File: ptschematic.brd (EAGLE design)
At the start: 100 x 80 mm, 28 parts, among them U3 NCP1117LPST33T3G, U4 BGM13S, Y2 32MHz

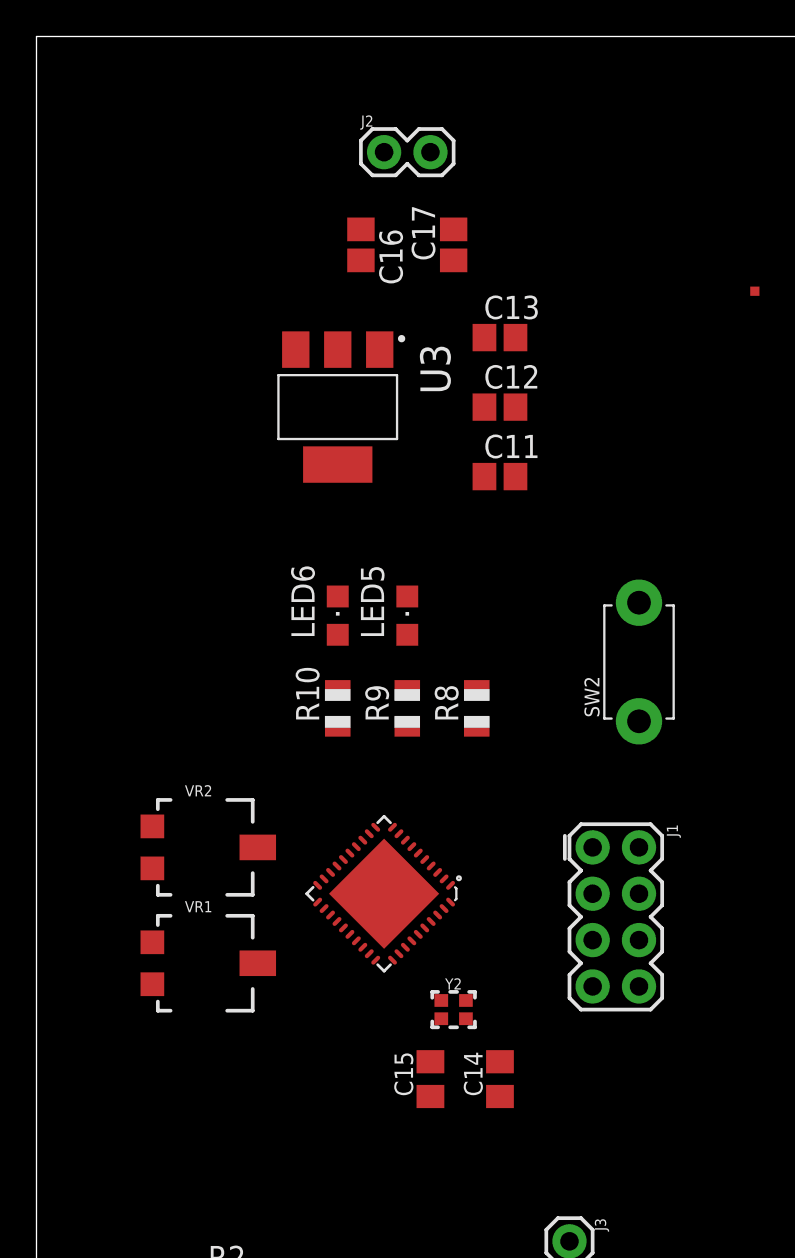
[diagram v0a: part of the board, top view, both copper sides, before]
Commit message: Started board routing
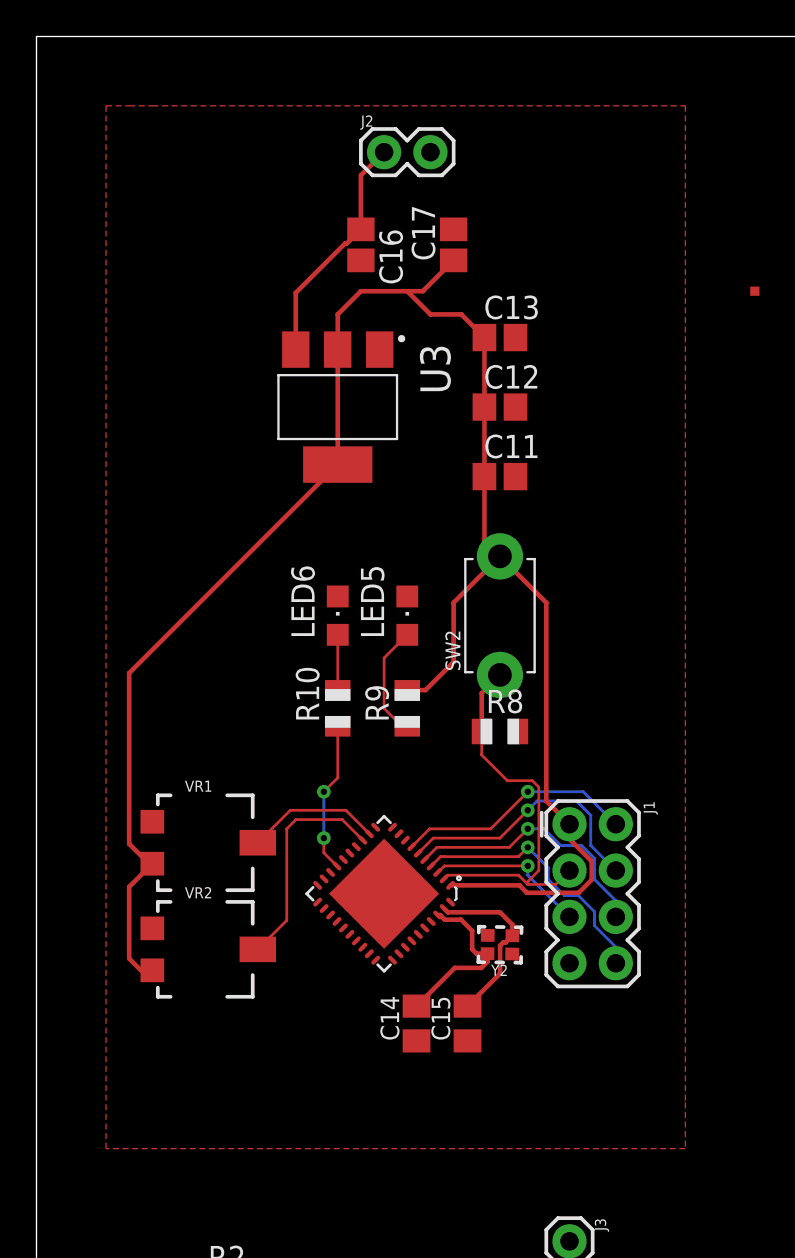
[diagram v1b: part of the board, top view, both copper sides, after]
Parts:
- moved SW2 8.03 mm to (25.4, 48.3)
- moved VR1 6.60 mm to (8.89, 35.8)
- moved VR2 5.59 mm to (8.89, 30.0)
- moved C14 5.49 mm to (20.8, 25.9)
- moved Y2 4.37 mm to (25.4, 30.2), turned to 179.2 degrees
- moved C15 3.66 mm to (23.6, 25.9)
- moved J1 1.80 mm to (30.5, 33.0)
- moved R8 1.80 mm to (25.4, 41.9), turned to 0 degrees
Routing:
- net 3.3V: track 0.00 -> 107.3 mm
- net RST: track 0.00 -> 21.7 mm
- net TDI: track 0.00 -> 14.6 mm, vias 0 -> 1
- net TCK: track 0.00 -> 14.5 mm, vias 0 -> 1
- net TMS: track 0.00 -> 14.4 mm, vias 0 -> 1
- net TDO/TDI: track 0.00 -> 13.2 mm, vias 0 -> 1
- net VIN: track 0.00 -> 12.9 mm
- net ADC2: track 0.00 -> 12.1 mm
- net N$16: track 0.00 -> 9.67 mm
- net N$11: track 0.00 -> 9.55 mm
- net TEST: track 0.00 -> 8.83 mm, vias 0 -> 1
- net N$17: track 0.00 -> 8.25 mm, vias 0 -> 2
- net ADC1: track 0.00 -> 7.38 mm
- net N$10: track 0.00 -> 6.62 mm
- net N$18: track 0.00 -> 3.03 mm
- added copper zone on layer 1, net GND

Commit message: finished tracing BGM
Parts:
- removed R1, R2: 0, adafruit:R0805
- moved TP3 60.6 mm to (8.38, 14.0)
- moved TP1 55.2 mm to (7.11, 14.0)
- moved TP4 54.1 mm to (8.38, 28.2)
- moved TP2 44.7 mm to (7.11, 28.2)
- moved J2 28.3 mm to (8.38, 47.5), turned to 180 degrees
- moved C17 26.1 mm to (14.4, 43.9), turned to 180 degrees
- moved J3 24.0 mm to (5.33, 11.2)
- moved U3 21.6 mm to (7.62, 40.0)
- moved C16 21.2 mm to (14.4, 47.6), turned to 0 degrees
- moved C13 19.1 mm to (18.5, 45.7), turned to 90 degrees
- moved C12 14.4 mm to (21.8, 45.7), turned to 90 degrees
- moved J1 12.0 mm to (29.5, 21.1)
- moved U$1 12.0 mm to (18.0, 21.1)
- moved VR2 12.0 mm to (7.87, 18.0)
- moved C14 12.0 mm to (19.8, 14.0)
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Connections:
- removed net ANT_GND: U4.P$47
- removed net N$5: R1.2, U4.P$2
- removed net N$6: R1.1, R2.1, U4.P$3
- net ADC1: now also TP4.P$1
- net ADC2: now also TP3.P$1
- net GND: now also U4.P$2, U4.P$3, U4.P$47; no longer R2.2, TP3.P$1, TP4.P$1
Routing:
- net A1RXD: track 0.00 -> 23.9 mm, vias 0 -> 2
- net A1TXD: track 0.00 -> 22.0 mm
- net BGMRST: track 0.00 -> 21.2 mm, vias 0 -> 2
- net GND: track 0.00 -> 18.9 mm, vias 0 -> 7
- net N$4: track 0.00 -> 17.1 mm, vias 0 -> 1
- net 3.3V: track 107.3 -> 124.5 mm
- net N$3: track 0.00 -> 15.9 mm
- net N$1: track 0.00 -> 14.3 mm, vias 0 -> 2
- net N$2: track 0.00 -> 13.6 mm
- net ADC1: track 7.38 -> 12.8 mm
- net ADC2: track 12.1 -> 17.4 mm
- net VIN: track 12.9 -> 10.8 mm
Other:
- board size 100 x 80 mm -> 33.5 x 51.6 mm

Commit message: updated board and schematic
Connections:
- net 3.3V: now also U$1.10
- net ADC1: now also U$1.11; no longer U$1.12
- net GND: now also U$1.12
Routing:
- net 3.3V: track 124.5 -> 133.2 mm
- net GND: track 18.9 -> 24.9 mm, vias 7 -> 11
- net ADC1: track 12.8 -> 13.5 mm
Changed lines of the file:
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@@
 <wire x1="10.707" y1="43.942" x2="9.92" y2="43.155" width="0.254" layer="16"/>
 <via x="9.92" y="43.155" extent="1-16" drill="0.25"/>
+<contactref element="U$1" pad="12"/>
+<wire x1="17.220825" y1="24.37004375" x2="16.62428125" y2="24.9665875" width="0.254" layer="1"/>
+<wire x1="16.62428125" y1="24.9665875" x2="16.62428125" y2="25.26028125" width="0.254" layer="1"/>
+<via x="16.62428125" y="25.26028125" extent="1-16" drill="0.25"/>
+<wire x1="16.62428125" y1="25.26028125" x2="17.78" y2="26.416" width="0.254" layer="16"/>
+<via x="17.78" y="26.416" extent="1-16" drill="0.25"/>
+<via x="25.384" y="29.972" extent="1-16" drill="0.25"/>
+<wire x1="25.384" y1="29.972" x2="25.892" y2="30.48" width="0.254" layer="16"/>
+<wire x1="25.892" y1="30.48" x2="28.448" y2="30.48" width="0.254" layer="16"/>
+<via x="28.448" y="30.48" extent="1-16" drill="0.25"/>
 </signal>
 <signal name="VIN">
@@
 <signal name="ADC1">
 <contactref element="VR1" pad="B"/>
-<contactref element="U$1" pad="12"/>
-<wire x1="11.1125" y1="23.876" x2="12.8905" y2="25.654" width="0.1524" layer="1"/>
-<wire x1="15.93686875" y1="25.654" x2="17.220825" y2="24.37004375" width="0.1524" layer="1"/>
-<wire x1="12.8905" y1="25.654" x2="15.93686875" y2="25.654" width="0.1524" layer="1"/>
 <contactref element="TP4" pad="P$1"/>
+<wire x1="12.8905" y1="25.654" x2="11.1125" y2="23.876" width="0.1524" layer="1"/>
 <wire x1="8.382" y1="28.194" x2="11.1125" y2="25.4635" width="0.254" layer="1"/>
 <wire x1="11.1125" y1="25.4635" x2="11.1125" y2="23.876" width="0.254" layer="1"/>
+<contactref element="U$1" pad="11"/>
+<wire x1="12.8905" y1="25.654" x2="15.494" y2="25.654" width="0.1524" layer="1"/>
+<wire x1="15.494" y1="25.654" x2="15.748" y2="25.908" width="0.1524" layer="1"/>
+<wire x1="15.748" y1="25.908" x2="16.764" y2="25.908" width="0.1524" layer="1"/>
+<wire x1="17.272" y1="25.4" x2="16.764" y2="25.908" width="0.1524" layer="1"/>
+<wire x1="17.574378125" y1="24.723596875" x2="17.272" y2="25.025975" width="0.1524" layer="1"/>
+<wire x1="17.272" y1="25.025975" x2="17.272" y2="25.4" width="0.1524" layer="1"/>
 </signal>
 <signal name="ADC2">
@@
 <wire x1="25.146" y1="43.434" x2="24.384" y2="42.672" width="0.254" layer="1"/>
 <wire x1="24.384" y1="42.672" x2="24.384" y2="39.572" width="0.254" layer="1"/>
+<contactref element="U$1" pad="10"/>
+<wire x1="18.49361875" y1="24.723596875" x2="20.32" y2="26.549978125" width="0.254" layer="1"/>
+<wire x1="20.32" y1="31.226" x2="19.304" y2="32.242" width="0.254" layer="1"/>
+<wire x1="20.32" y1="26.549978125" x2="20.32" y2="31.226" width="0.254" layer="1"/>
 </signal>
 </signals>

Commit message: final updated with BOM
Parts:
- removed SW2: (no value), adafruit:TACT_PANA-EVQ
- added S1: MOMENTARY-SWITCH-SPST-SMD-6.2MM-TALL, SparkFun-Switches:TACTILE_SWITCH_SMD_6.2MM_TALL
- C14, C15: value 22pF -> 10pf
- moved LED5 2.54 mm to (16.8, 36.3)
- moved LED6 2.54 mm to (13.0, 36.3)
- moved R10 2.54 mm to (13.0, 31.2)
- moved R9 2.54 mm to (16.8, 31.2)
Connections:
- net 3.3V: now also S1.B2; no longer SW2.P$2
- net RST: now also S1.A2; no longer SW2.P$1
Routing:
- net 3.3V: track 133.2 -> 138.5 mm
- net RST: track 21.7 -> 25.8 mm
- net N$17: track 8.25 -> 9.23 mm
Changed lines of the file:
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@@
 <element name="C12" library="adafruit" package="C0805" value="4.7uF" x="21.844" y="45.72" rot="R90"/>
 <element name="C13" library="adafruit" package="C0805" value="4.7uF" x="18.542" y="45.72" rot="R90"/>
-<element name="C14" library="cap-master" package="0805" value="22pF" x="19.812" y="13.97" rot="R90"/>
-<element name="C15" library="cap-master" package="0805" value="22pF" x="22.606" y="13.97" rot="R90"/>
+<element name="C14" library="cap-master" package="0805" value="10pf" x="19.812" y="13.97" rot="R90"/>
+<element name="C15" library="cap-master" package="0805" value="10pf" x="22.606" y="13.97" rot="R90"/>
 <element name="C16" library="adafruit" package="C0805" value="10 uF" x="14.351" y="47.625"/>
 <element name="C17" library="adafruit" package="C0805" value="10 uF" x="14.351" y="43.942" rot="R180"/>
@@
 <attribute name="PROD_ID" value="CONN-09696" x="5.334" y="11.176" size="1.778" layer="27" rot="R270" display="off"/>
 </element>
-<element name="LED5" library="adafruit" package="CHIPLED_0805" value="" x="19.304" y="36.322"/>
-<element name="LED6" library="adafruit" package="CHIPLED_0805" value="" x="15.494" y="36.322"/>
-<element name="R10" library="adafruit" package="R0805" value="680" x="15.494" y="31.242" rot="R90"/>
+<element name="LED5" library="adafruit" package="CHIPLED_0805" value="" x="16.764" y="36.322"/>
+<element name="LED6" library="adafruit" package="CHIPLED_0805" value="" x="12.954" y="36.322"/>
+<element name="R10" library="adafruit" package="R0805" value="680" x="12.954" y="31.242" rot="R90"/>
 <element name="R8" library="adafruit" package="R0805" value="680" x="24.384" y="29.972"/>
-<element name="R9" library="adafruit" package="R0805" value="680" x="19.304" y="31.242" rot="R90"/>
-<element name="SW2" library="adafruit" package="TACT_PANA-EVQ" value="" x="24.384" y="36.322" rot="R90"/>
+<element name="R9" library="adafruit" package="R0805" value="680" x="16.764" y="31.242" rot="R90"/>
 <element name="TP1" library="SparkFun-Connectors" package="PAD.02X.02" value="TEST-POINT2" x="7.112" y="13.97"/>
 <element name="TP2" library="SparkFun-Connectors" package="PAD.02X.02" value="TEST-POINT2" x="7.112" y="28.194"/>
@@
 <element name="Y2" library="SparkFun-Clocks" library_urn="urn:adsk.eagle:library:511" package="CRYSTAL-SMD-2.0X1.6MM" package3d_urn="urn:adsk.eagle:package:37531/1" value="32MHz" x="24.384" y="18.288" rot="R179.2">
 <attribute name="PROD_ID" value="XTAL-13459" x="24.384" y="18.288" size="1.778" layer="27" rot="R179.2" display="off"/>
+</element>
+<element name="S1" library="SparkFun-Switches" library_urn="urn:adsk.eagle:library:535" package="TACTILE_SWITCH_SMD_6.2MM_TALL" package3d_urn="urn:adsk.eagle:package:40172/1" value="MOMENTARY-SWITCH-SPST-SMD-6.2MM-TALL" x="23.368" y="38.1">
+<attribute name="PROD_ID" value="SWCH-11966" x="23.368" y="38.1" size="1.778" layer="27" display="off"/>
+<attribute name="SF_SKU" value="COM-12992" x="23.368" y="38.1" size="1.778" layer="27" display="off"/>
 </element>
 </elements>
@@
 <signal name="RST">
 <contactref element="U$1" pad="2"/>
-<contactref element="SW2" pad="P$1"/>
 <contactref element="R8" pad="1"/>
 <contactref element="J1" pad="3"/>
-<wire x1="24.384" y1="33.072" x2="23.384" y2="32.072" width="0.254" layer="1"/>
-<wire x1="23.384" y1="32.072" x2="23.384" y2="29.972" width="0.254" layer="1"/>
+<wire x1="23.384" y1="29.972" x2="23.384" y2="32.072" width="0.254" layer="1"/>
 <wire x1="21.32204375" y1="21.895171875" x2="21.524871875" y2="22.098" width="0.1524" layer="1"/>
 <wire x1="25.4" y1="22.098" x2="25.908" y2="21.59" width="0.1524" layer="1"/>
@@
 <wire x1="23.368" y1="28.702" x2="23.384" y2="28.718" width="0.1524" layer="1"/>
 <wire x1="23.384" y1="28.718" x2="23.384" y2="29.972" width="0.1524" layer="1"/>
+<contactref element="S1" pad="A2"/>
+<wire x1="27.162" y1="35.85" x2="27.343" y2="35.85" width="0.254" layer="1"/>
+<wire x1="23.384" y1="32.072" x2="27.162" y2="35.85" width="0.254" layer="1"/>
 </signal>
 <signal name="N$11">
@@
 <contactref element="R9" pad="1"/>
 <contactref element="LED5" pad="A"/>
-<wire x1="19.304" y1="35.272" x2="18.034" y2="34.002" width="0.1524" layer="1"/>
-<wire x1="18.034" y1="34.002" x2="18.034" y2="31.242" width="0.1524" layer="1"/>
-<wire x1="18.034" y1="31.242" x2="19.304" y2="29.972" width="0.1524" layer="1"/>
-<wire x1="19.304" y1="29.972" x2="19.304" y2="30.242" width="0.1524" layer="1"/>
+<wire x1="16.764" y1="30.242" x2="17.542" y2="30.242" width="0.254" layer="1"/>
+<wire x1="17.542" y1="30.242" x2="18.288" y2="30.988" width="0.254" layer="1"/>
+<wire x1="18.288" y1="30.988" x2="18.288" y2="34.036" width="0.254" layer="1"/>
+<wire x1="17.052" y1="35.272" x2="16.764" y2="35.272" width="0.254" layer="1"/>
+<wire x1="18.288" y1="34.036" x2="17.052" y2="35.272" width="0.254" layer="1"/>
 </signal>
 <signal name="ADC1">
@@
 <contactref element="R10" pad="1"/>
 <contactref element="U$1" pad="17"/>
-<wire x1="15.494" y1="30.242" x2="15.494" y2="27.432" width="0.1524" layer="1"/>
+<wire x1="12.954" y1="30.242" x2="15.494" y2="27.432" width="0.1524" layer="1"/>
 <wire x1="15.494" y1="27.432" x2="14.732" y2="26.67" width="0.1524" layer="1"/>
 <via x="14.732" y="26.67" extent="1-16" drill="0.35"/>
@@
 <contactref element="R10" pad="2"/>
 <contactref element="LED6" pad="A"/>
-<wire x1="15.494" y1="35.272" x2="15.494" y2="32.242" width="0.1524" layer="1"/>
+<wire x1="12.954" y1="35.272" x2="12.954" y2="32.242" width="0.1524" layer="1"/>
 </signal>
 <signal name="BGMRST">
@@
 <contactref element="C11" pad="1"/>
 <contactref element="U$1" pad="1"/>
-<contactref element="SW2" pad="P$2"/>
 <contactref element="U4" pad="P$24"/>
 <contactref element="U4" pad="P$22"/>
-<wire x1="24.384" y1="39.572" x2="21.844" y2="37.032" width="0.254" layer="1"/>
-<wire x1="21.844" y1="37.032" x2="21.844" y2="33.782" width="0.254" layer="1"/>
-<wire x1="21.844" y1="33.782" x2="20.304" y2="32.242" width="0.254" layer="1"/>
-<wire x1="20.304" y1="32.242" x2="19.304" y2="32.242" width="0.254" layer="1"/>
-<wire x1="24.384" y1="39.572" x2="26.924" y2="37.032" width="0.254" layer="1"/>
-<wire x1="26.924" y1="37.032" x2="26.924" y2="26.162" width="0.254" layer="1"/>
-<wire x1="26.924" y1="26.162" x2="28.194" y2="24.892" width="0.254" layer="1"/>
+<wire x1="28.194" y1="24.892" x2="26.924" y2="26.162" width="0.254" layer="1"/>
 <wire x1="28.6990125" y1="21.1328" x2="29.4132" y2="21.8469875" width="0.254" layer="1"/>
 <wire x1="29.4132" y1="21.8469875" x2="29.4132" y2="22.8570125" width="0.254" layer="1"/>
@@
 <wire x1="21.844" y1="44.87" x2="25.146" y2="44.87" width="0.254" layer="1"/>
 <wire x1="25.146" y1="44.87" x2="25.146" y2="43.434" width="0.254" layer="1"/>
-<wire x1="25.146" y1="43.434" x2="24.384" y2="42.672" width="0.254" layer="1"/>
-<wire x1="24.384" y1="42.672" x2="24.384" y2="39.572" width="0.254" layer="1"/>
 <contactref element="U$1" pad="10"/>
-<wire x1="18.49361875" y1="24.723596875" x2="20.32" y2="26.549978125" width="0.254" layer="1"/>
-<wire x1="20.32" y1="31.226" x2="19.304" y2="32.242" width="0.254" layer="1"/>
-<wire x1="20.32" y1="26.549978125" x2="20.32" y2="31.226" width="0.254" layer="1"/>
+<wire x1="18.49361875" y1="24.723596875" x2="20.253009375" y2="26.4829875" width="0.254" layer="1"/>
+<contactref element="S1" pad="B2"/>
+<wire x1="20.253009375" y1="26.4829875" x2="20.32" y2="26.549978125" width="0.254" layer="1"/>
+<wire x1="25.146" y1="43.434" x2="27.343" y2="41.237" width="0.254" layer="1"/>
+<wire x1="27.343" y1="41.237" x2="27.343" y2="40.35" width="0.254" layer="1"/>
+<wire x1="14.732" y1="42.164" x2="14.732" y2="34.274" width="0.254" layer="1"/>
+<wire x1="14.732" y1="34.274" x2="16.764" y2="32.242" width="0.254" layer="1"/>
+<wire x1="20.253009375" y1="26.4829875" x2="18.287996875" y2="28.448" width="0.254" layer="1"/>
+<wire x1="18.287996875" y1="28.448" x2="16.256" y2="28.448" width="0.254" layer="1"/>
+<wire x1="16.256" y1="28.448" x2="15.24" y2="29.464" width="0.254" layer="1"/>
+<wire x1="15.24" y1="29.464" x2="15.24" y2="30.718" width="0.254" layer="1"/>
+<wire x1="15.24" y1="30.718" x2="16.764" y2="32.242" width="0.254" layer="1"/>
+<wire x1="26.924" y1="26.162" x2="26.924" y2="33.02" width="0.254" layer="1"/>
+<wire x1="26.924" y1="33.02" x2="28.956" y2="35.052" width="0.254" layer="1"/>
+<wire x1="28.956" y1="35.052" x2="28.956" y2="36.576" width="0.254" layer="1"/>
+<wire x1="27.343" y1="38.189" x2="27.343" y2="40.35" width="0.254" layer="1"/>
+<wire x1="28.956" y1="36.576" x2="27.343" y2="38.189" width="0.254" layer="1"/>
 </signal>
 </signals>
